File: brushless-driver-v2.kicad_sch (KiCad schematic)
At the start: 52 parts, among them J1 Conn_01x07_Socket, J2 encoder, J3 motor, U1 TCMT1100, U2 TCMT1100, U3 TCMT1100, U5 L7805

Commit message: Updated Footprint of JST connector to 2mm pitch
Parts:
- J1: footprint Connector_JST:JST_EH_S7B-EH_1x07_P2.50mm_Horizontal -> Connector_JST:JST_PH_S7B-PH-K_1x07_P2.00mm_Horizontal
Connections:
- net +5V: now also J1.1 (Pin_1); no longer J1.7 (Pin_7)
- net DIR: now also J1.3 (Pin_3); no longer J1.5 (Pin_5)
- net GND: now also J1.7 (Pin_7); no longer J1.1 (Pin_1)
- net RX: now also J1.6 (Pin_6); no longer J1.2 (Pin_2)
- net THR: now also J1.2 (Pin_2); no longer J1.6 (Pin_6)
- net TX: now also J1.5 (Pin_5); no longer J1.3 (Pin_3)
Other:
- moved on the sheet: J1
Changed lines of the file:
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@@
 	(symbol
 		(lib_id "Connector:Conn_01x07_Socket")
-		(at 38.1 50.8 0)
-		(mirror y)
+		(at 38.1 50.8 180)
 		(unit 1)
 		(exclude_from_sim no)
@@
 		(dnp no)
 		(property "Reference" "J1"
-			(at 38.735 63.5 0)
+			(at 38.735 38.1 0)
 			(effects
 				(font
@@
 		)
 		(property "Value" "Conn_01x07_Socket"
-			(at 38.735 60.96 0)
+			(at 38.735 40.64 0)
 			(effects
 				(font
@@
 			)
 		)
-		(property "Footprint" "Connector_JST:JST_EH_S7B-EH_1x07_P2.50mm_Horizontal"
+		(property "Footprint" "Connector_JST:JST_PH_S7B-PH-K_1x07_P2.00mm_Horizontal"
 			(at 38.1 50.8 0)
 			(effects

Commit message: Improvements, more to be done
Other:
- note added: "2do: 10k seriell an jeden input"
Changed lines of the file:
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@@
 	(generator_version "9.0")
 	(paper "A4")
+	(text "2do:\n10k seriell an jeden input\n"
+		(exclude_from_sim no)
+		(at 41.91 145.034 0)
+		(effects
+			(font
+				(size 1.27 1.27)
+			)
+		)
+	)
 	(junction
 		(at 109.22 29.21)

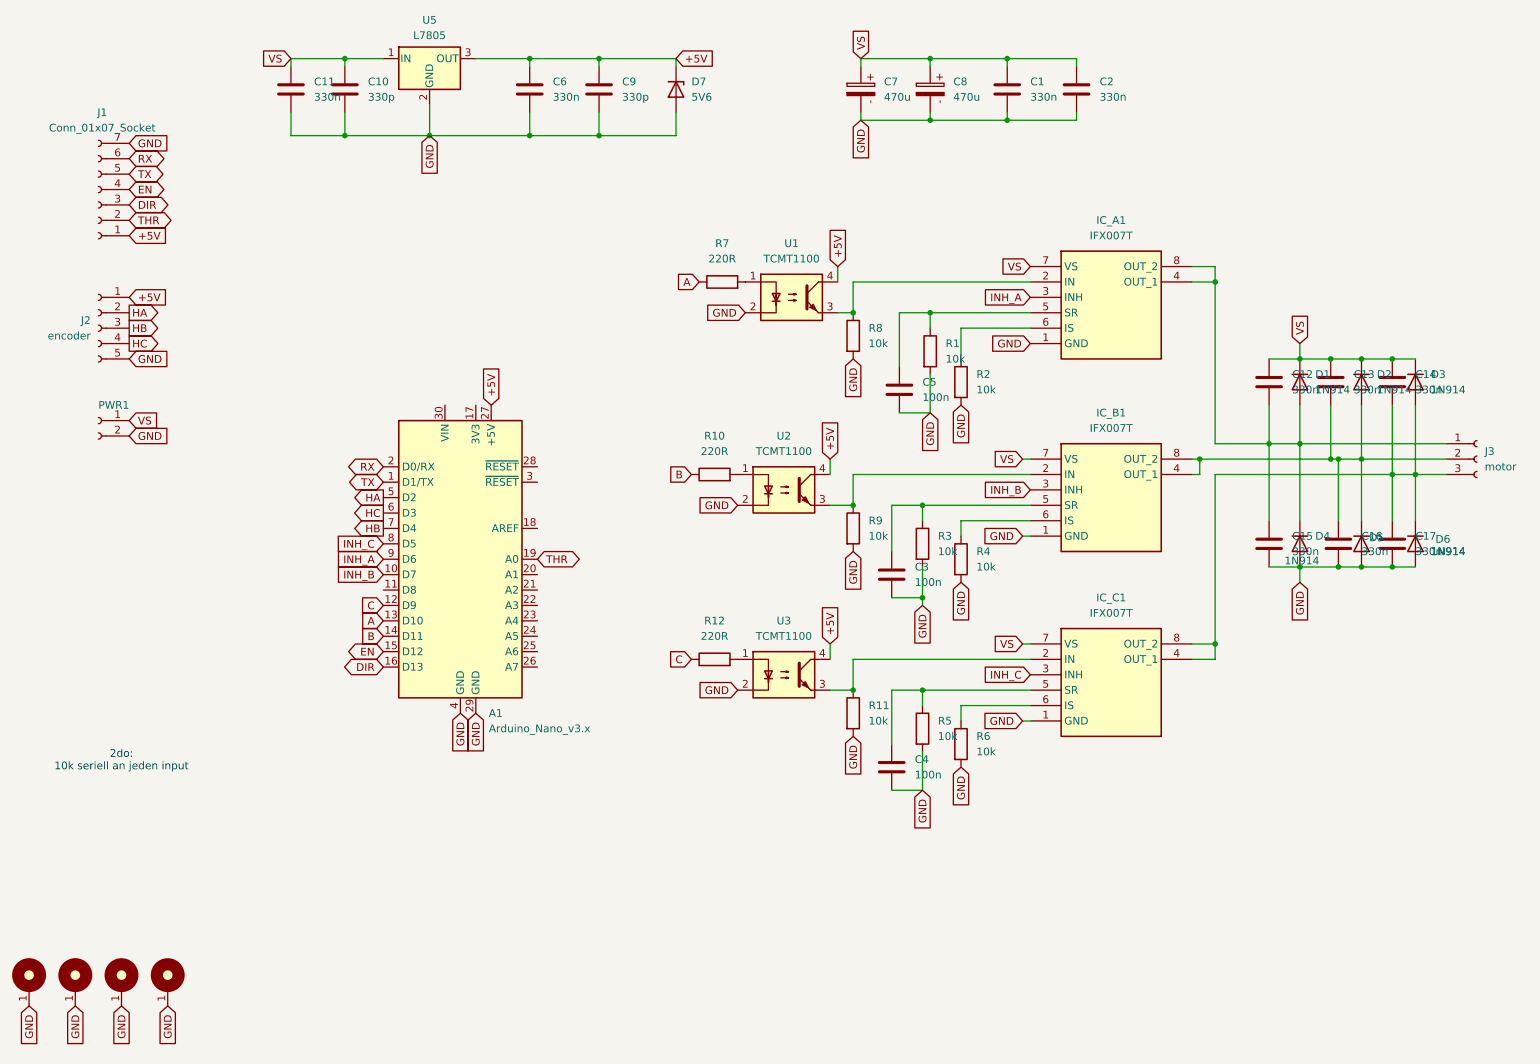
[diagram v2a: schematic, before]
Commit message: Started on version 3. Major redesign according to dev board for the IFX007T. Previous version was unfit for continous operation - now zones instead of traces for high current lines.
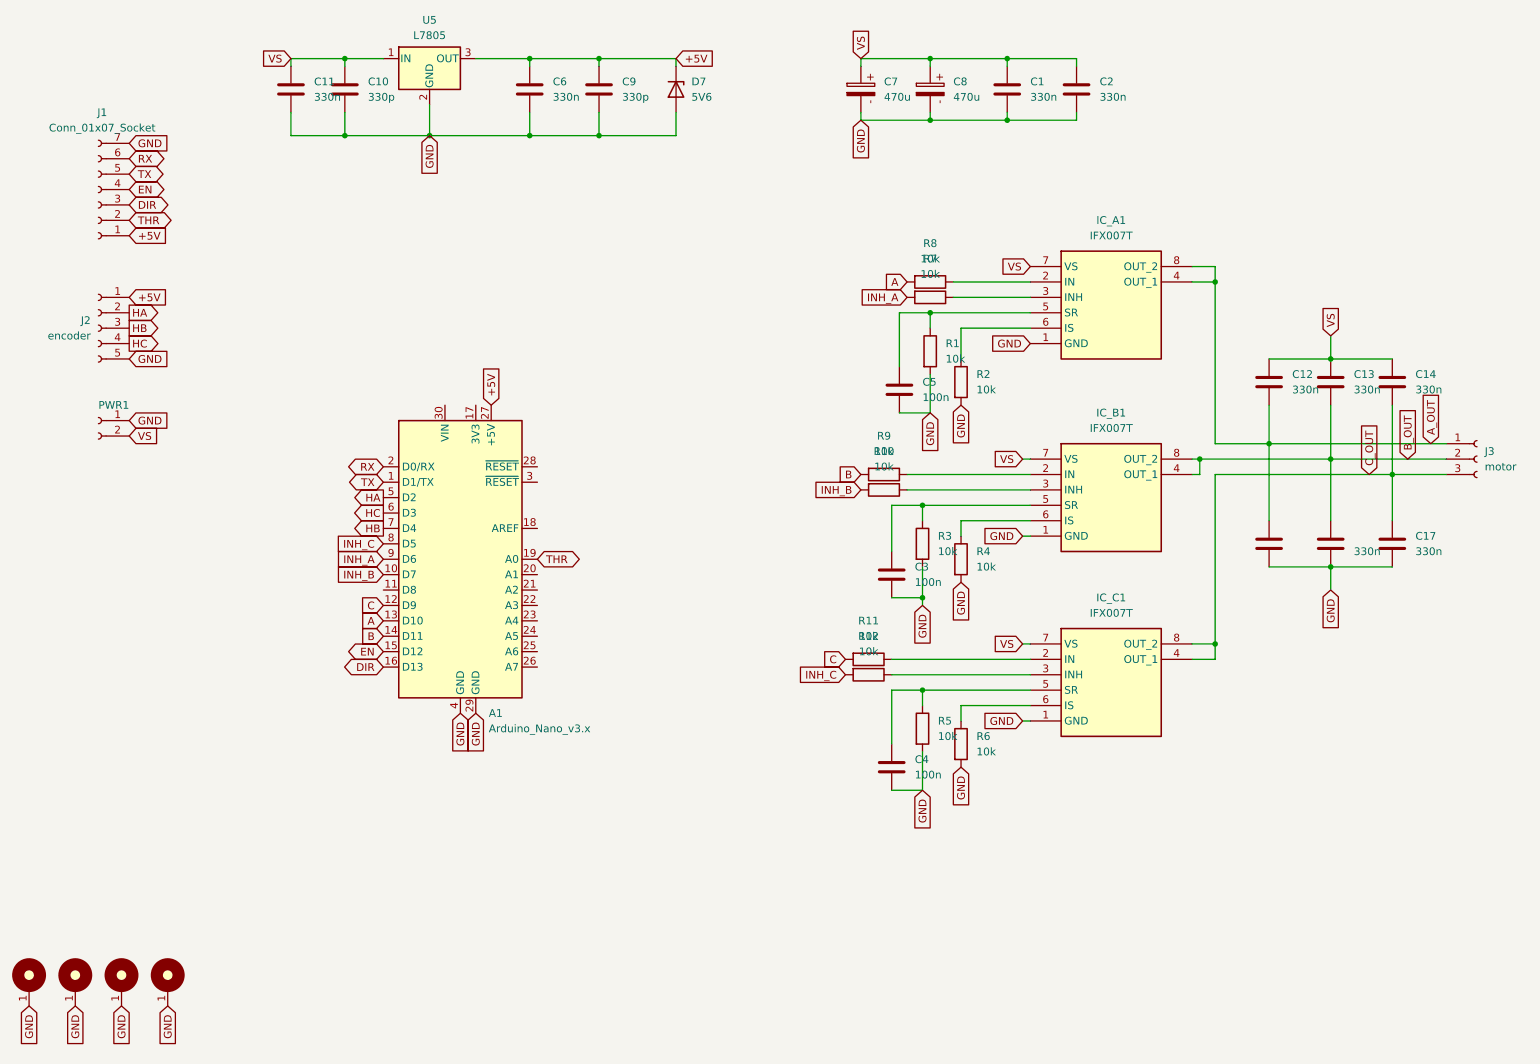
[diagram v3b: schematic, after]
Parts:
- removed D1, D2, D3, D4, D5, D6: 1N914, Diode_THT:D_DO-35_SOD27_P7.62mm_Horizontal, symbol Diode:1N914
- removed U1, U2, U3: TCMT1100, meiBib:SOP-4_4.4x2.6mm_P1.27mm, symbol Isolator:TCMT1100
- R10, R12, R7: value 220R -> 10k
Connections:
- net A: now also R8.2; no longer R7.1
- net B: now also R9.2; no longer R10.1
- net C: now also R11.2; no longer R12.1
- net GND: now also PWR1.1 (Pin_1); no longer PWR1.2 (Pin_2), R11.2, R8.2, R9.2
- net INH_A: now also R7.2; no longer IC_A1.3 (INH)
- net INH_B: now also R10.2; no longer IC_B1.3 (INH)
- net INH_C: now also R12.2; no longer IC_C1.3 (INH)
- net VS: now also PWR1.2 (Pin_2); no longer PWR1.1 (Pin_1)
- net B_OUT: now reaches C13.2, C16.1, IC_B1.4 (OUT_1), IC_B1.8 (OUT_2), J3.2 (Pin_2)
- net A_OUT: now reaches C12.2, C15.1, IC_A1.4 (OUT_1), IC_A1.8 (OUT_2), J3.1 (Pin_1)
- net C_OUT: now reaches C14.2, C17.1, IC_C1.4 (OUT_1), IC_C1.8 (OUT_2), J3.3 (Pin_3)
- new net: IC_A1.3 (INH), R7.1
- new net: IC_C1.3 (INH), R12.1
- new net: IC_B1.3 (INH), R10.1
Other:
- note removed: "2do: 10k seriell an jeden input"
- moved on the sheet: R11, R8, R9

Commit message: finished rework
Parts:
- removed C12, C13, C14, C15, C16, C17: 330n, Capacitor_SMD:C_0805_2012Metric_Pad1.18x1.45mm_HandSolder, symbol Device:C
- R1, R3, R5: value 10k -> 5k6

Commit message: Improvements to routing of power signals
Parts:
- D7: footprint Diode_SMD:Nexperia_CFP3_SOD-123W -> meiBib:SOD-123W
- U5: footprint Package_TO_SOT_SMD:TO-252-2 -> meiBib:SOT-223-3_TabPin2
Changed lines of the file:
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@@
 			)
 		)
-		(property "Footprint" "Package_TO_SOT_SMD:TO-252-2"
+		(property "Footprint" "meiBib:SOT-223-3_TabPin2"
 			(at 93.345 33.02 0)
 			(effects
@@
 			)
 		)
-		(property "Footprint" "Diode_SMD:Nexperia_CFP3_SOD-123W"
+		(property "Footprint" "meiBib:SOD-123W"
 			(at 133.35 34.29 0)
 			(effects

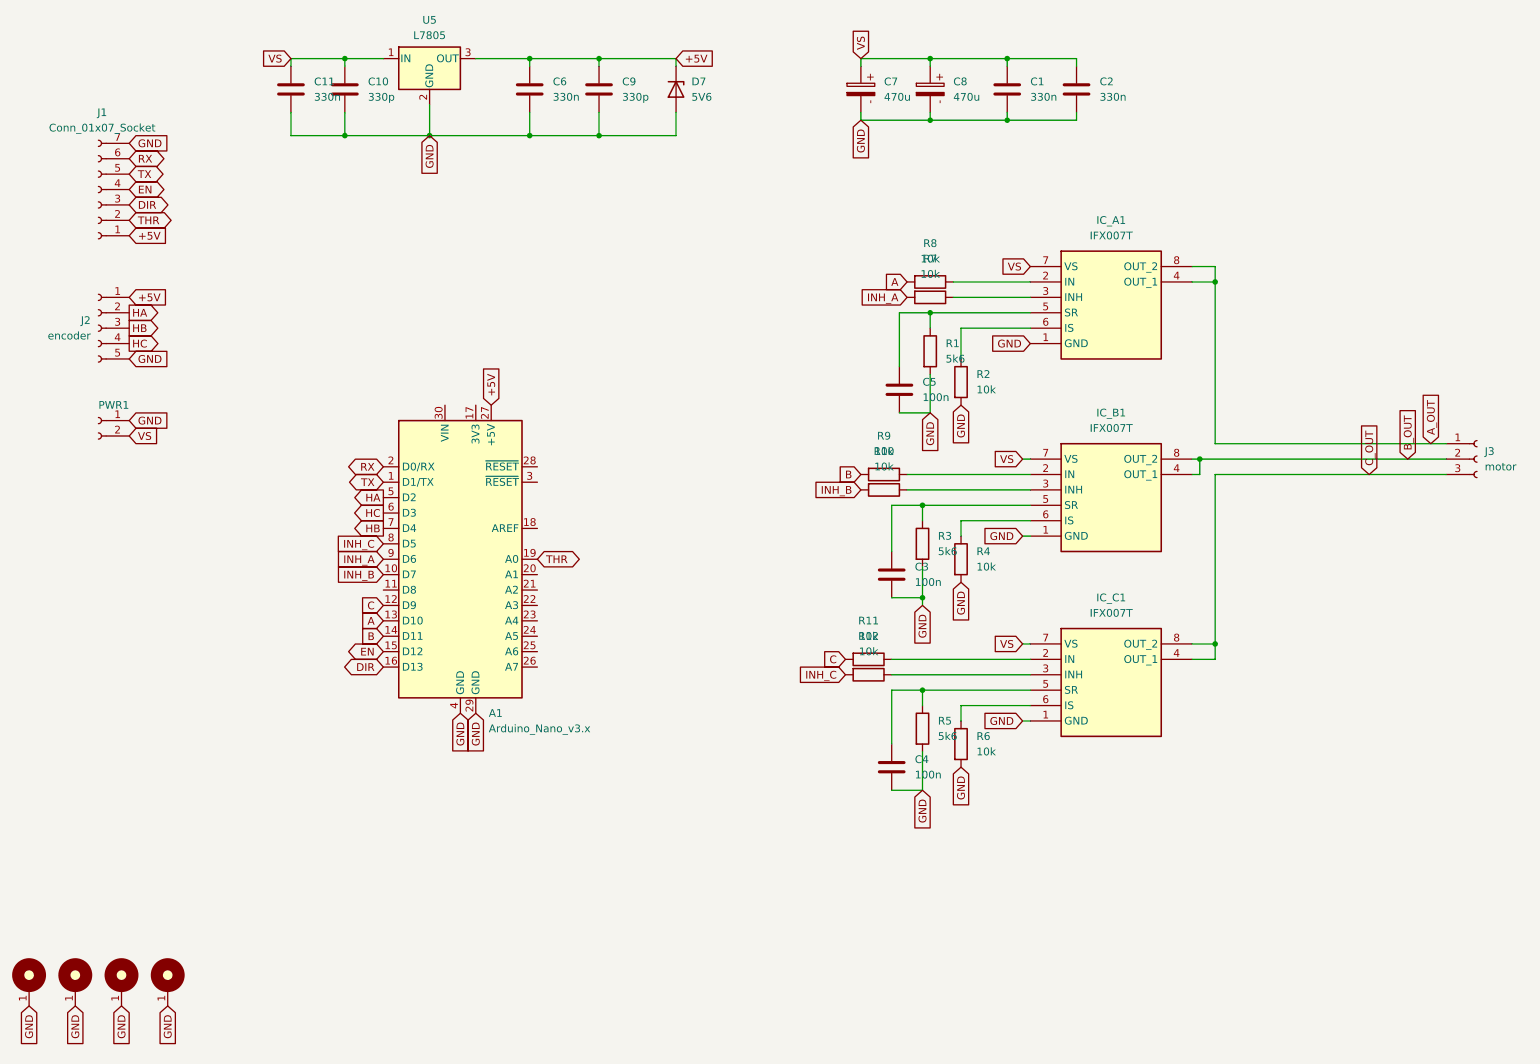
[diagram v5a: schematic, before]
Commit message: Started on second power stage, broke first power stage
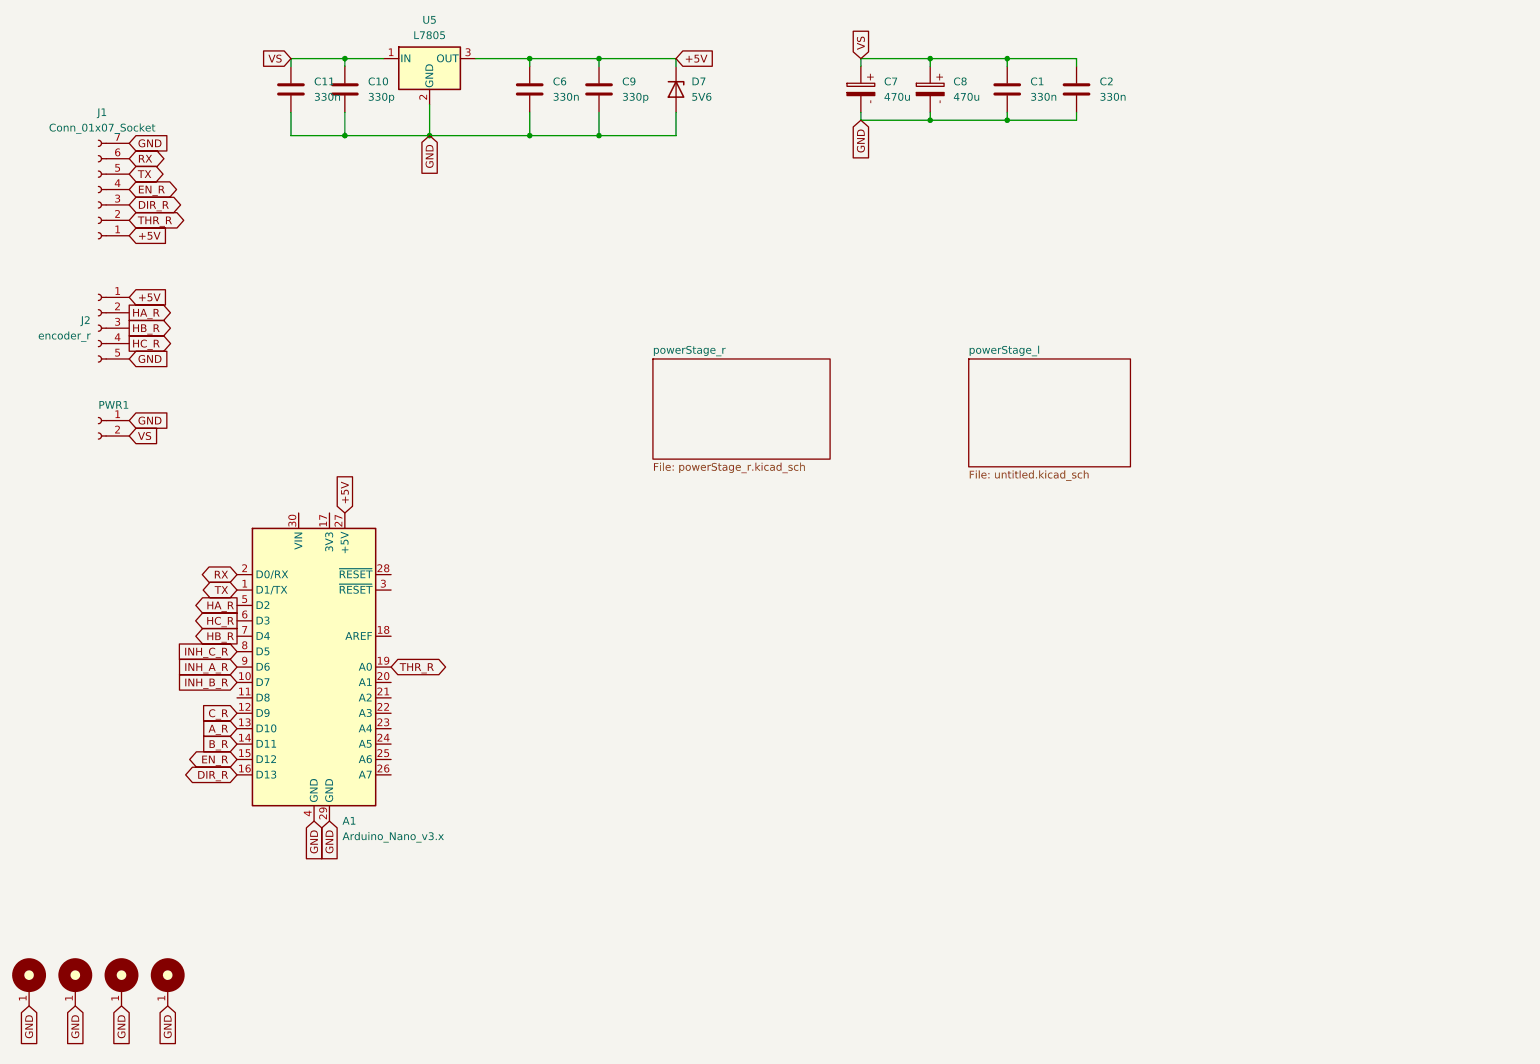
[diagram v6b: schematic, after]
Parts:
- removed C3, C4, C5: 100n, Capacitor_SMD:C_0805_2012Metric_Pad1.18x1.45mm_HandSolder, symbol Device:C
- removed IC_A1, IC_B1, IC_C1: IFX007T, myLib:PG-TO263-7-1, symbol myLib:IFX007T
- removed J3: motor, TerminalBlock:TerminalBlock_MaiXu_MX126-5.0-03P_1x03_P5.00mm, symbol Connector:Conn_01x03_Socket
- removed R1, R3, R5: 5k6, Resistor_SMD:R_0805_2012Metric_Pad1.20x1.40mm_HandSolder, symbol myLib:R
- removed R10, R11, R12, R2, R4, R6, R7, R8, R9: 10k, Resistor_SMD:R_0805_2012Metric_Pad1.20x1.40mm_HandSolder, symbol myLib:R
- J2: value encoder -> encoder_r
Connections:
- net A renamed A_R
- net B renamed B_R
- net C renamed C_R
- net DIR renamed DIR_R
- net EN renamed EN_R
- net HA renamed HA_R
- net HB renamed HB_R
- net HC renamed HC_R
- net INH_A renamed INH_A_R
- net INH_B renamed INH_B_R
- net INH_C renamed INH_C_R
- net THR renamed THR_R
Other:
- added sheet powerStage_l (untitled.kicad_sch)
- added sheet powerStage_r (powerStage_r.kicad_sch)
- moved on the sheet: A1
